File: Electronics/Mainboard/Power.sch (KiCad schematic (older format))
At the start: 7 parts

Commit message: Layout progress
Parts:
- removed TP1: TestPoint, TestPoint:TestPoint_Pad_D1.5mm, symbol Connector:TestPoint
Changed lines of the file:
@@
 	2250 4650 3100 4650
-$Comp
-L Connector:TestPoint TP1
-U 1 1 5EDB0C69
-P 2450 1150
-F 0 "TP1" H 2508 1268 50  0001 L CNN
-F 1 "TestPoint" H 2508 1177 50  0001 L CNN
-F 2 "TestPoint:TestPoint_Pad_D1.5mm" H 2650 1150 50  0001 C CNN
-F 3 "~" H 2650 1150 50  0001 C CNN
-	1    2450 1150
-	1    0    0    -1
-$EndComp
 $Comp
 L Device:CP_Small C77

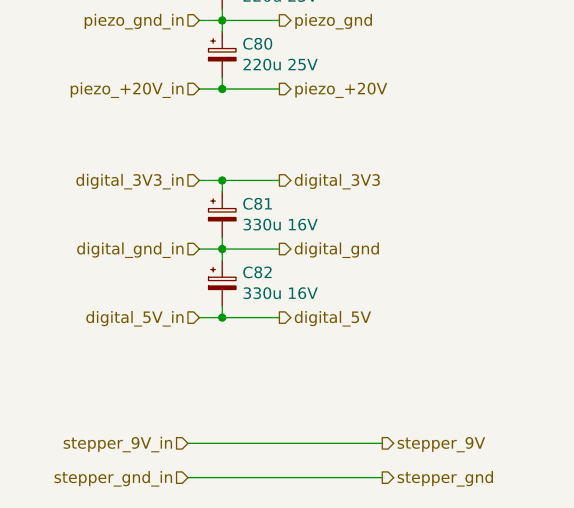
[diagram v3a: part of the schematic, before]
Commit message: Power supply routing progress
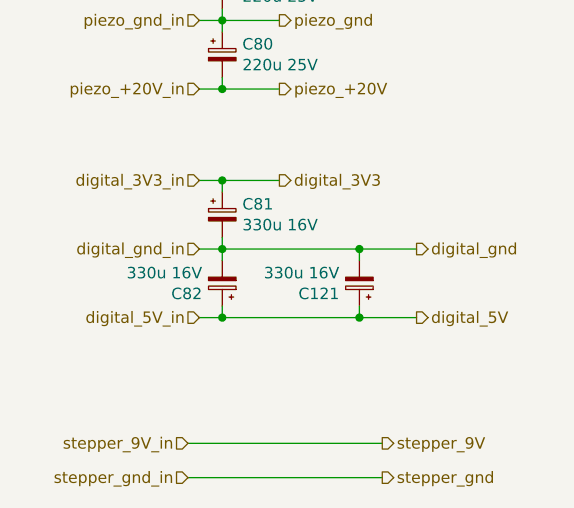
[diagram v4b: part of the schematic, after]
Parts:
- added C121: 330u 16V, Capacitor_THT:CP_Radial_D8.0mm_P3.50mm, symbol Device:CP_Small
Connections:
- net digital_5V: now also C82.1, C121.1; no longer C82.2
- net digital_gnd: now also C82.2, C121.2; no longer C82.1
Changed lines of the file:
@@
 Text HLabel 2650 3350 2    50   Output ~ 0
 digital_3V3
-Text HLabel 2650 3650 2    50   Output ~ 0
+Text HLabel 3250 3650 2    50   Output ~ 0
 digital_gnd
-Text HLabel 2650 3950 2    50   Output ~ 0
+Text HLabel 3250 3950 2    50   Output ~ 0
 digital_5V
 Text HLabel 2250 4500 0    50   Input ~ 0
@@
 	2650 3350 2400 3350
 Wire Wire Line
-	2650 3650 2400 3650
+	3250 3650 3000 3650
 Wire Wire Line
 	2300 3950 2400 3950
@@
 Connection ~ 2400 3950
 Wire Wire Line
-	2400 3950 2650 3950
+	2400 3950 3000 3950
 $Comp
 L Device:CP_Small C82
@@
 F 4 "493-1042-ND" H 2400 3800 50  0001 C CNN "Digikey"
 	1    2400 3800
-	1    0    0    -1
+	-1   0    0    1
 $EndComp
+$Comp
+L Device:CP_Small C121
+U 1 1 5EFE479A
+P 3000 3800
+F 0 "C121" H 3088 3846 50  0000 L CNN
+F 1 "330u 16V" H 3088 3755 50  0000 L CNN
+F 2 "Capacitor_THT:CP_Radial_D8.0mm_P3.50mm" H 3000 3800 50  0001 C CNN
+F 3 "~" H 3000 3800 50  0001 C CNN
+F 4 "493-1042-ND" H 3000 3800 50  0001 C CNN "Digikey"
+	1    3000 3800
+	-1   0    0    1
+$EndComp
+Wire Wire Line
+	3000 3900 3000 3950
+Connection ~ 3000 3950
+Wire Wire Line
+	3000 3950 3250 3950
+Wire Wire Line
+	3000 3700 3000 3650
+Connection ~ 3000 3650
+Wire Wire Line
+	3000 3650 2400 3650
 $EndSCHEMATC

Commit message: Layout nearly finished
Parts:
- added C122, C123, C124, C125, C126, C127, C128, C129, C130, C131, C132, C133, C134, C135, C136, C137: 1u, Capacitor_SMD:C_1210_3225Metric_Pad1.42x2.65mm_HandSolder, symbol Device:C_Small
- added TP10, TP12, TP13, TP7, TP8, TP9: TestPoint, TestPoint:TestPoint_Loop_D1.80mm_Drill1.0mm_Beaded, symbol Connector:TestPoint
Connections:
- net analog_+15V: now also C123.2, C125.2, C127.2, C129.2, C131.2, C135.2, C136.2, C137.2, TP8.1
- net analog_-15V: now also C122.1, C124.1, C126.1, C128.1, C130.1, C132.1, C133.1, C134.1, TP7.1
- net analog_gnd: now also C122.2, C123.1, C124.2, C125.1, C126.2, C127.1, C128.2, C129.1, C130.2, C131.1, C132.2, C133.2, C134.2, C135.1, C136.1, C137.1
- net digital_5V: now also TP13.1
- net piezo_+20V: now also TP10.1
- net piezo_-20V: now also TP9.1
- net stepper_9V: now also TP12.1

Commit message: Mainboard layout and schematic done
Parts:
- C122, C123, C124, C125, C126, C127, C128, C129, C130, C131, C132, C133, C134, C135, C136, C137: value 1u -> 10u; footprint Capacitor_SMD:C_1210_3225Metric_Pad1.42x2.65mm_HandSolder -> Capacitor_SMD:C_1206_3216Metric
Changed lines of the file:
@@
 P 3250 1450
 F 0 "C122" H 3342 1496 50  0000 L CNN
-F 1 "1u" H 3342 1405 50  0000 L CNN
-F 2 "Capacitor_SMD:C_1210_3225Metric_Pad1.42x2.65mm_HandSolder" H 3250 1450 50  0001 C CNN
+F 1 "10u" H 3342 1405 50  0000 L CNN
+F 2 "Capacitor_SMD:C_1206_3216Metric" H 3250 1450 50  0001 C CNN
 F 3 "~" H 3250 1450 50  0001 C CNN
 F 4 "445-13027-1-ND" H 3250 1450 50  0001 C CNN "Digikey"
+F 5 "" H 3250 1450 50  0001 C CNN "LCSC"
 	1    3250 1450
 	1    0    0    -1
@@
 P 3250 1750
 F 0 "C123" H 3342 1796 50  0000 L CNN
-F 1 "1u" H 3342 1705 50  0000 L CNN
-F 2 "Capacitor_SMD:C_1210_3225Metric_Pad1.42x2.65mm_HandSolder" H 3250 1750 50  0001 C CNN
+F 1 "10u" H 3342 1705 50  0000 L CNN
+F 2 "Capacitor_SMD:C_1206_3216Metric" H 3250 1750 50  0001 C CNN
 F 3 "~" H 3250 1750 50  0001 C CNN
 F 4 "445-13027-1-ND" H 3250 1750 50  0001 C CNN "Digikey"
+F 5 "" H 3250 1750 50  0001 C CNN "LCSC"
 	1    3250 1750
 	1    0    0    -1
@@
 P 3600 1450
 F 0 "C124" H 3692 1496 50  0000 L CNN
-F 1 "1u" H 3692 1405 50  0000 L CNN
-F 2 "Capacitor_SMD:C_1210_3225Metric_Pad1.42x2.65mm_HandSolder" H 3600 1450 50  0001 C CNN
+F 1 "10u" H 3692 1405 50  0000 L CNN
+F 2 "Capacitor_SMD:C_1206_3216Metric" H 3600 1450 50  0001 C CNN
 F 3 "~" H 3600 1450 50  0001 C CNN
 F 4 "445-13027-1-ND" H 3600 1450 50  0001 C CNN "Digikey"
+F 5 "" H 3600 1450 50  0001 C CNN "LCSC"
 	1    3600 1450
 	1    0    0    -1
@@
 P 3600 1750
 F 0 "C125" H 3692 1796 50  0000 L CNN
-F 1 "1u" H 3692 1705 50  0000 L CNN
-F 2 "Capacitor_SMD:C_1210_3225Metric_Pad1.42x2.65mm_HandSolder" H 3600 1750 50  0001 C CNN
+F 1 "10u" H 3692 1705 50  0000 L CNN
+F 2 "Capacitor_SMD:C_1206_3216Metric" H 3600 1750 50  0001 C CNN
 F 3 "~" H 3600 1750 50  0001 C CNN
 F 4 "445-13027-1-ND" H 3600 1750 50  0001 C CNN "Digikey"
+F 5 "" H 3600 1750 50  0001 C CNN "LCSC"
 	1    3600 1750
 	1    0    0    -1
@@
 P 4300 1450
 F 0 "C128" H 4392 1496 50  0000 L CNN
-F 1 "1u" H 4392 1405 50  0000 L CNN
-F 2 "Capacitor_SMD:C_1210_3225Metric_Pad1.42x2.65mm_HandSolder" H 4300 1450 50  0001 C CNN
+F 1 "10u" H 4392 1405 50  0000 L CNN
+F 2 "Capacitor_SMD:C_1206_3216Metric" H 4300 1450 50  0001 C CNN
 F 3 "~" H 4300 1450 50  0001 C CNN
 F 4 "445-13027-1-ND" H 4300 1450 50  0001 C CNN "Digikey"
+F 5 "" H 4300 1450 50  0001 C CNN "LCSC"
 	1    4300 1450
 	1    0    0    -1
@@
 P 4300 1750
 F 0 "C129" H 4392 1796 50  0000 L CNN
-F 1 "1u" H 4392 1705 50  0000 L CNN
-F 2 "Capacitor_SMD:C_1210_3225Metric_Pad1.42x2.65mm_HandSolder" H 4300 1750 50  0001 C CNN
+F 1 "10u" H 4392 1705 50  0000 L CNN
+F 2 "Capacitor_SMD:C_1206_3216Metric" H 4300 1750 50  0001 C CNN
 F 3 "~" H 4300 1750 50  0001 C CNN
 F 4 "445-13027-1-ND" H 4300 1750 50  0001 C CNN "Digikey"
+F 5 "" H 4300 1750 50  0001 C CNN "LCSC"
 	1    4300 1750
 	1    0    0    -1
@@
 P 4650 1450
 F 0 "C130" H 4742 1496 50  0000 L CNN
-F 1 "1u" H 4742 1405 50  0000 L CNN
-F 2 "Capacitor_SMD:C_1210_3225Metric_Pad1.42x2.65mm_HandSolder" H 4650 1450 50  0001 C CNN
+F 1 "10u" H 4742 1405 50  0000 L CNN
+F 2 "Capacitor_SMD:C_1206_3216Metric" H 4650 1450 50  0001 C CNN
 F 3 "~" H 4650 1450 50  0001 C CNN
 F 4 "445-13027-1-ND" H 4650 1450 50  0001 C CNN "Digikey"
+F 5 "" H 4650 1450 50  0001 C CNN "LCSC"
 	1    4650 1450
 	1    0    0    -1
@@
 P 4650 1750
 F 0 "C131" H 4742 1796 50  0000 L CNN
-F 1 "1u" H 4742 1705 50  0000 L CNN
-F 2 "Capacitor_SMD:C_1210_3225Metric_Pad1.42x2.65mm_HandSolder" H 4650 1750 50  0001 C CNN
+F 1 "10u" H 4742 1705 50  0000 L CNN
+F 2 "Capacitor_SMD:C_1206_3216Metric" H 4650 1750 50  0001 C CNN
 F 3 "~" H 4650 1750 50  0001 C CNN
 F 4 "445-13027-1-ND" H 4650 1750 50  0001 C CNN "Digikey"
+F 5 "" H 4650 1750 50  0001 C CNN "LCSC"
 	1    4650 1750
 	1    0    0    -1
@@
 P 3950 1750
 F 0 "C127" H 4042 1796 50  0000 L CNN
-F 1 "1u" H 4042 1705 50  0000 L CNN
-F 2 "Capacitor_SMD:C_1210_3225Metric_Pad1.42x2.65mm_HandSolder" H 3950 1750 50  0001 C CNN
+F 1 "10u" H 4042 1705 50  0000 L CNN
+F 2 "Capacitor_SMD:C_1206_3216Metric" H 3950 1750 50  0001 C CNN
 F 3 "~" H 3950 1750 50  0001 C CNN
 F 4 "445-13027-1-ND" H 3950 1750 50  0001 C CNN "Digikey"
+F 5 "" H 3950 1750 50  0001 C CNN "LCSC"
 	1    3950 1750
 	1    0    0    -1
@@
 P 3950 1450
 F 0 "C126" H 4042 1496 50  0000 L CNN
-F 1 "1u" H 4042 1405 50  0000 L CNN
-F 2 "Capacitor_SMD:C_1210_3225Metric_Pad1.42x2.65mm_HandSolder" H 3950 1450 50  0001 C CNN
+F 1 "10u" H 4042 1405 50  0000 L CNN
+F 2 "Capacitor_SMD:C_1206_3216Metric" H 3950 1450 50  0001 C CNN
 F 3 "~" H 3950 1450 50  0001 C CNN
 F 4 "445-13027-1-ND" H 3950 1450 50  0001 C CNN "Digikey"
+F 5 "" H 3950 1450 50  0001 C CNN "LCSC"
 	1    3950 1450
 	1    0    0    -1
@@
 P 5350 1450
 F 0 "C133" H 5442 1496 50  0000 L CNN
-F 1 "1u" H 5442 1405 50  0000 L CNN
-F 2 "Capacitor_SMD:C_1210_3225Metric_Pad1.42x2.65mm_HandSolder" H 5350 1450 50  0001 C CNN
+F 1 "10u" H 5442 1405 50  0000 L CNN
+F 2 "Capacitor_SMD:C_1206_3216Metric" H 5350 1450 50  0001 C CNN
 F 3 "~" H 5350 1450 50  0001 C CNN
 F 4 "445-13027-1-ND" H 5350 1450 50  0001 C CNN "Digikey"
+F 5 "" H 5350 1450 50  0001 C CNN "LCSC"
 	1    5350 1450
 	1    0    0    -1
@@
 P 5700 1450
 F 0 "C134" H 5792 1496 50  0000 L CNN
-F 1 "1u" H 5792 1405 50  0000 L CNN
-F 2 "Capacitor_SMD:C_1210_3225Metric_Pad1.42x2.65mm_HandSolder" H 5700 1450 50  0001 C CNN
+F 1 "10u" H 5792 1405 50  0000 L CNN
+F 2 "Capacitor_SMD:C_1206_3216Metric" H 5700 1450 50  0001 C CNN
 F 3 "~" H 5700 1450 50  0001 C CNN
 F 4 "445-13027-1-ND" H 5700 1450 50  0001 C CNN "Digikey"
+F 5 "" H 5700 1450 50  0001 C CNN "LCSC"
 	1    5700 1450
 	1    0    0    -1
@@
 P 5000 1450
 F 0 "C132" H 5092 1496 50  0000 L CNN
-F 1 "1u" H 5092 1405 50  0000 L CNN
-F 2 "Capacitor_SMD:C_1210_3225Metric_Pad1.42x2.65mm_HandSolder" H 5000 1450 50  0001 C CNN
+F 1 "10u" H 5092 1405 50  0000 L CNN
+F 2 "Capacitor_SMD:C_1206_3216Metric" H 5000 1450 50  0001 C CNN
 F 3 "~" H 5000 1450 50  0001 C CNN
 F 4 "445-13027-1-ND" H 5000 1450 50  0001 C CNN "Digikey"
+F 5 "" H 5000 1450 50  0001 C CNN "LCSC"
 	1    5000 1450
 	1    0    0    -1
@@
 P 5350 1750
 F 0 "C136" H 5442 1796 50  0000 L CNN
-F 1 "1u" H 5442 1705 50  0000 L CNN
-F 2 "Capacitor_SMD:C_1210_3225Metric_Pad1.42x2.65mm_HandSolder" H 5350 1750 50  0001 C CNN
+F 1 "10u" H 5442 1705 50  0000 L CNN
+F 2 "Capacitor_SMD:C_1206_3216Metric" H 5350 1750 50  0001 C CNN
 F 3 "~" H 5350 1750 50  0001 C CNN
 F 4 "445-13027-1-ND" H 5350 1750 50  0001 C CNN "Digikey"
+F 5 "" H 5350 1750 50  0001 C CNN "LCSC"
 	1    5350 1750
 	1    0    0    -1
@@
 P 5700 1750
 F 0 "C137" H 5792 1796 50  0000 L CNN
-F 1 "1u" H 5792 1705 50  0000 L CNN
-F 2 "Capacitor_SMD:C_1210_3225Metric_Pad1.42x2.65mm_HandSolder" H 5700 1750 50  0001 C CNN
+F 1 "10u" H 5792 1705 50  0000 L CNN
+F 2 "Capacitor_SMD:C_1206_3216Metric" H 5700 1750 50  0001 C CNN
 F 3 "~" H 5700 1750 50  0001 C CNN
 F 4 "445-13027-1-ND" H 5700 1750 50  0001 C CNN "Digikey"
+F 5 "" H 5700 1750 50  0001 C CNN "LCSC"
 	1    5700 1750
 	1    0    0    -1
@@
 P 5000 1750
 F 0 "C135" H 5092 1796 50  0000 L CNN
-F 1 "1u" H 5092 1705 50  0000 L CNN
-F 2 "Capacitor_SMD:C_1210_3225Metric_Pad1.42x2.65mm_HandSolder" H 5000 1750 50  0001 C CNN
+F 1 "10u" H 5092 1705 50  0000 L CNN
+F 2 "Capacitor_SMD:C_1206_3216Metric" H 5000 1750 50  0001 C CNN
 F 3 "~" H 5000 1750 50  0001 C CNN
 F 4 "445-13027-1-ND" H 5000 1750 50  0001 C CNN "Digikey"
+F 5 "" H 5000 1750 50  0001 C CNN "LCSC"
 	1    5000 1750
 	1    0    0    -1

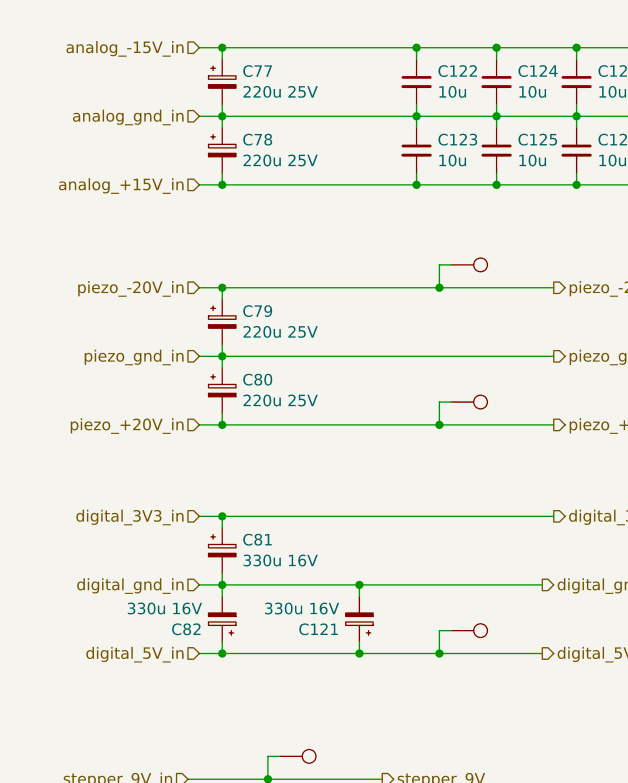
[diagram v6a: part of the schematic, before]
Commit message: Added images
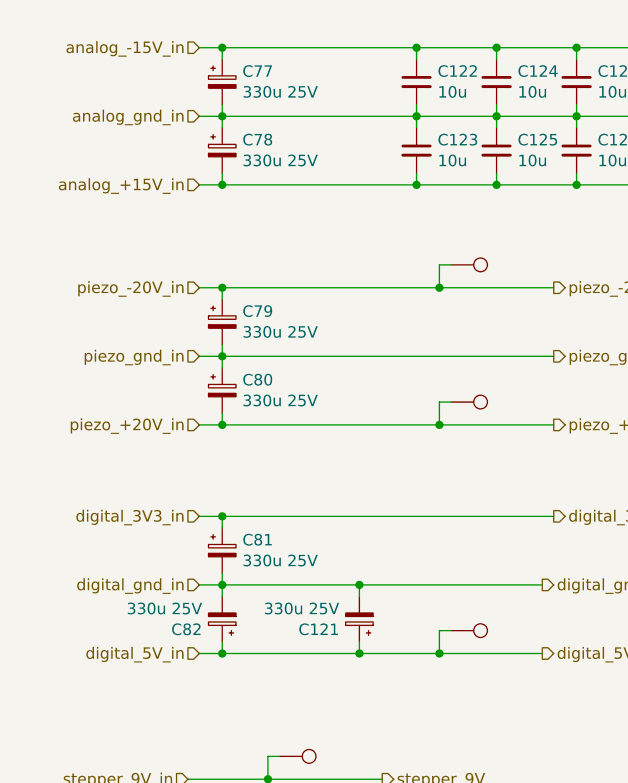
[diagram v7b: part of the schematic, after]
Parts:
- C121, C81, C82: value 330u 16V -> 330u 25V; Digikey 493-1042-ND -> (none); Reichelt (none) -> RAD FR 330/25
- C122, C123, C124, C125, C126, C127, C128, C129, C130, C131, C132, C133, C134, C135, C136, C137: Digikey 445-13027-1-ND -> (none); Reichelt (none) -> RND 1501206B475K
- C77, C78, C79, C80: value 220u 25V -> 330u 25V; Digikey 493-5914-1-ND -> (none); Reichelt (none) -> RAD FR 330/25
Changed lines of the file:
@@
 P 2400 1450
 F 0 "C77" H 2488 1496 50  0000 L CNN
-F 1 "220u 25V" H 2488 1405 50  0000 L CNN
+F 1 "330u 25V" H 2488 1405 50  0000 L CNN
 F 2 "Capacitor_THT:CP_Radial_D8.0mm_P3.50mm" H 2400 1450 50  0001 C CNN
 F 3 "~" H 2400 1450 50  0001 C CNN
-F 4 "493-5914-1-ND" H 2400 1450 50  0001 C CNN "Digikey"
+F 4 "" H 2400 1450 50  0001 C CNN "Digikey"
+F 5 "RAD FR 330/25" H 2400 1450 50  0001 C CNN "Reichelt"
 	1    2400 1450
 	1    0    0    -1
@@
 P 2400 1750
 F 0 "C78" H 2488 1796 50  0000 L CNN
-F 1 "220u 25V" H 2488 1705 50  0000 L CNN
+F 1 "330u 25V" H 2488 1705 50  0000 L CNN
 F 2 "Capacitor_THT:CP_Radial_D8.0mm_P3.50mm" H 2400 1750 50  0001 C CNN
 F 3 "~" H 2400 1750 50  0001 C CNN
-F 4 "493-5914-1-ND" H 2400 1750 50  0001 C CNN "Digikey"
+F 4 "" H 2400 1750 50  0001 C CNN "Digikey"
+F 5 "RAD FR 330/25" H 2400 1750 50  0001 C CNN "Reichelt"
 	1    2400 1750
 	1    0    0    -1
@@
 P 2400 2500
 F 0 "C79" H 2488 2546 50  0000 L CNN
-F 1 "220u 25V" H 2488 2455 50  0000 L CNN
+F 1 "330u 25V" H 2488 2455 50  0000 L CNN
 F 2 "Capacitor_THT:CP_Radial_D8.0mm_P3.50mm" H 2400 2500 50  0001 C CNN
 F 3 "~" H 2400 2500 50  0001 C CNN
-F 4 "493-5914-1-ND" H 2400 2500 50  0001 C CNN "Digikey"
+F 4 "" H 2400 2500 50  0001 C CNN "Digikey"
+F 5 "RAD FR 330/25" H 2400 2500 50  0001 C CNN "Reichelt"
 	1    2400 2500
 	1    0    0    -1
@@
 P 2400 2800
 F 0 "C80" H 2488 2846 50  0000 L CNN
-F 1 "220u 25V" H 2488 2755 50  0000 L CNN
+F 1 "330u 25V" H 2488 2755 50  0000 L CNN
 F 2 "Capacitor_THT:CP_Radial_D8.0mm_P3.50mm" H 2400 2800 50  0001 C CNN
 F 3 "~" H 2400 2800 50  0001 C CNN
-F 4 "493-5914-1-ND" H 2400 2800 50  0001 C CNN "Digikey"
+F 4 "" H 2400 2800 50  0001 C CNN "Digikey"
+F 5 "RAD FR 330/25" H 2400 2800 50  0001 C CNN "Reichelt"
 	1    2400 2800
 	1    0    0    -1
@@
 P 2400 3500
 F 0 "C81" H 2488 3546 50  0000 L CNN
-F 1 "330u 16V" H 2488 3455 50  0000 L CNN
+F 1 "330u 25V" H 2488 3455 50  0000 L CNN
 F 2 "Capacitor_THT:CP_Radial_D8.0mm_P3.50mm" H 2400 3500 50  0001 C CNN
 F 3 "~" H 2400 3500 50  0001 C CNN
-F 4 "493-1042-ND" H 2400 3500 50  0001 C CNN "Digikey"
+F 4 "" H 2400 3500 50  0001 C CNN "Digikey"
+F 5 "RAD FR 330/25" H 2400 3500 50  0001 C CNN "Reichelt"
 	1    2400 3500
 	1    0    0    -1
@@
 P 2400 3800
 F 0 "C82" H 2488 3846 50  0000 L CNN
-F 1 "330u 16V" H 2488 3755 50  0000 L CNN
+F 1 "330u 25V" H 2488 3755 50  0000 L CNN
 F 2 "Capacitor_THT:CP_Radial_D8.0mm_P3.50mm" H 2400 3800 50  0001 C CNN
 F 3 "~" H 2400 3800 50  0001 C CNN
-F 4 "493-1042-ND" H 2400 3800 50  0001 C CNN "Digikey"
+F 4 "" H 2400 3800 50  0001 C CNN "Digikey"
+F 5 "RAD FR 330/25" H 2400 3800 50  0001 C CNN "Reichelt"
 	1    2400 3800
 	-1   0    0    1
@@
 P 3000 3800
 F 0 "C121" H 3088 3846 50  0000 L CNN
-F 1 "330u 16V" H 3088 3755 50  0000 L CNN
+F 1 "330u 25V" H 3088 3755 50  0000 L CNN
 F 2 "Capacitor_THT:CP_Radial_D8.0mm_P3.50mm" H 3000 3800 50  0001 C CNN
 F 3 "~" H 3000 3800 50  0001 C CNN
-F 4 "493-1042-ND" H 3000 3800 50  0001 C CNN "Digikey"
+F 4 "" H 3000 3800 50  0001 C CNN "Digikey"
+F 5 "RAD FR 330/25" H 3000 3800 50  0001 C CNN "Reichelt"
 	1    3000 3800
 	-1   0    0    1
@@
 F 2 "Capacitor_SMD:C_1206_3216Metric" H 3250 1450 50  0001 C CNN
 F 3 "~" H 3250 1450 50  0001 C CNN
-F 4 "445-13027-1-ND" H 3250 1450 50  0001 C CNN "Digikey"
+F 4 "" H 3250 1450 50  0001 C CNN "Digikey"
 F 5 "" H 3250 1450 50  0001 C CNN "LCSC"
+F 6 "RND 1501206B475K" H 3250 1450 50  0001 C CNN "Reichelt"
 	1    3250 1450
 	1    0    0    -1
@@
 F 2 "Capacitor_SMD:C_1206_3216Metric" H 3250 1750 50  0001 C CNN
 F 3 "~" H 3250 1750 50  0001 C CNN
-F 4 "445-13027-1-ND" H 3250 1750 50  0001 C CNN "Digikey"
+F 4 "" H 3250 1750 50  0001 C CNN "Digikey"
 F 5 "" H 3250 1750 50  0001 C CNN "LCSC"
+F 6 "RND 1501206B475K" H 3250 1750 50  0001 C CNN "Reichelt"
 	1    3250 1750
 	1    0    0    -1
@@
 F 2 "Capacitor_SMD:C_1206_3216Metric" H 3600 1450 50  0001 C CNN
 F 3 "~" H 3600 1450 50  0001 C CNN
-F 4 "445-13027-1-ND" H 3600 1450 50  0001 C CNN "Digikey"
+F 4 "" H 3600 1450 50  0001 C CNN "Digikey"
 F 5 "" H 3600 1450 50  0001 C CNN "LCSC"
+F 6 "RND 1501206B475K" H 3600 1450 50  0001 C CNN "Reichelt"
 	1    3600 1450
 	1    0    0    -1
@@
 F 2 "Capacitor_SMD:C_1206_3216Metric" H 3600 1750 50  0001 C CNN
 F 3 "~" H 3600 1750 50  0001 C CNN
-F 4 "445-13027-1-ND" H 3600 1750 50  0001 C CNN "Digikey"
+F 4 "" H 3600 1750 50  0001 C CNN "Digikey"
 F 5 "" H 3600 1750 50  0001 C CNN "LCSC"
+F 6 "RND 1501206B475K" H 3600 1750 50  0001 C CNN "Reichelt"
 	1    3600 1750
 	1    0    0    -1
@@
 F 2 "Capacitor_SMD:C_1206_3216Metric" H 4300 1450 50  0001 C CNN
 F 3 "~" H 4300 1450 50  0001 C CNN
-F 4 "445-13027-1-ND" H 4300 1450 50  0001 C CNN "Digikey"
+F 4 "" H 4300 1450 50  0001 C CNN "Digikey"
 F 5 "" H 4300 1450 50  0001 C CNN "LCSC"
+F 6 "RND 1501206B475K" H 4300 1450 50  0001 C CNN "Reichelt"
 	1    4300 1450
 	1    0    0    -1
@@
 F 2 "Capacitor_SMD:C_1206_3216Metric" H 4300 1750 50  0001 C CNN
 F 3 "~" H 4300 1750 50  0001 C CNN
-F 4 "445-13027-1-ND" H 4300 1750 50  0001 C CNN "Digikey"
+F 4 "" H 4300 1750 50  0001 C CNN "Digikey"
 F 5 "" H 4300 1750 50  0001 C CNN "LCSC"
+F 6 "RND 1501206B475K" H 4300 1750 50  0001 C CNN "Reichelt"
 	1    4300 1750
 	1    0    0    -1
@@
 F 2 "Capacitor_SMD:C_1206_3216Metric" H 4650 1450 50  0001 C CNN
 F 3 "~" H 4650 1450 50  0001 C CNN
-F 4 "445-13027-1-ND" H 4650 1450 50  0001 C CNN "Digikey"
+F 4 "" H 4650 1450 50  0001 C CNN "Digikey"
 F 5 "" H 4650 1450 50  0001 C CNN "LCSC"
+F 6 "RND 1501206B475K" H 4650 1450 50  0001 C CNN "Reichelt"
 	1    4650 1450
 	1    0    0    -1
@@
 F 2 "Capacitor_SMD:C_1206_3216Metric" H 4650 1750 50  0001 C CNN
 F 3 "~" H 4650 1750 50  0001 C CNN
-F 4 "445-13027-1-ND" H 4650 1750 50  0001 C CNN "Digikey"
+F 4 "" H 4650 1750 50  0001 C CNN "Digikey"
 F 5 "" H 4650 1750 50  0001 C CNN "LCSC"
+F 6 "RND 1501206B475K" H 4650 1750 50  0001 C CNN "Reichelt"
 	1    4650 1750
 	1    0    0    -1
@@
 F 2 "Capacitor_SMD:C_1206_3216Metric" H 3950 1750 50  0001 C CNN
 F 3 "~" H 3950 1750 50  0001 C CNN
-F 4 "445-13027-1-ND" H 3950 1750 50  0001 C CNN "Digikey"
+F 4 "" H 3950 1750 50  0001 C CNN "Digikey"
 F 5 "" H 3950 1750 50  0001 C CNN "LCSC"
+F 6 "RND 1501206B475K" H 3950 1750 50  0001 C CNN "Reichelt"
 	1    3950 1750
 	1    0    0    -1
@@
 F 2 "Capacitor_SMD:C_1206_3216Metric" H 3950 1450 50  0001 C CNN
 F 3 "~" H 3950 1450 50  0001 C CNN
-F 4 "445-13027-1-ND" H 3950 1450 50  0001 C CNN "Digikey"
+F 4 "" H 3950 1450 50  0001 C CNN "Digikey"
 F 5 "" H 3950 1450 50  0001 C CNN "LCSC"
+F 6 "RND 1501206B475K" H 3950 1450 50  0001 C CNN "Reichelt"
 	1    3950 1450
 	1    0    0    -1
@@
 F 2 "Capacitor_SMD:C_1206_3216Metric" H 5350 1450 50  0001 C CNN
 F 3 "~" H 5350 1450 50  0001 C CNN
-F 4 "445-13027-1-ND" H 5350 1450 50  0001 C CNN "Digikey"
+F 4 "" H 5350 1450 50  0001 C CNN "Digikey"
 F 5 "" H 5350 1450 50  0001 C CNN "LCSC"
+F 6 "RND 1501206B475K" H 5350 1450 50  0001 C CNN "Reichelt"
 	1    5350 1450
 	1    0    0    -1
@@
 F 2 "Capacitor_SMD:C_1206_3216Metric" H 5700 1450 50  0001 C CNN
 F 3 "~" H 5700 1450 50  0001 C CNN
-F 4 "445-13027-1-ND" H 5700 1450 50  0001 C CNN "Digikey"
+F 4 "" H 5700 1450 50  0001 C CNN "Digikey"
 F 5 "" H 5700 1450 50  0001 C CNN "LCSC"
+F 6 "RND 1501206B475K" H 5700 1450 50  0001 C CNN "Reichelt"
 	1    5700 1450
 	1    0    0    -1
@@
 F 2 "Capacitor_SMD:C_1206_3216Metric" H 5000 1450 50  0001 C CNN
 F 3 "~" H 5000 1450 50  0001 C CNN
-F 4 "445-13027-1-ND" H 5000 1450 50  0001 C CNN "Digikey"
+F 4 "" H 5000 1450 50  0001 C CNN "Digikey"
 F 5 "" H 5000 1450 50  0001 C CNN "LCSC"
+F 6 "RND 1501206B475K" H 5000 1450 50  0001 C CNN "Reichelt"
 	1    5000 1450
 	1    0    0    -1
@@
 F 2 "Capacitor_SMD:C_1206_3216Metric" H 5350 1750 50  0001 C CNN
 F 3 "~" H 5350 1750 50  0001 C CNN
-F 4 "445-13027-1-ND" H 5350 1750 50  0001 C CNN "Digikey"
+F 4 "" H 5350 1750 50  0001 C CNN "Digikey"
 F 5 "" H 5350 1750 50  0001 C CNN "LCSC"
+F 6 "RND 1501206B475K" H 5350 1750 50  0001 C CNN "Reichelt"
 	1    5350 1750
 	1    0    0    -1
@@
 F 2 "Capacitor_SMD:C_1206_3216Metric" H 5700 1750 50  0001 C CNN
 F 3 "~" H 5700 1750 50  0001 C CNN
-F 4 "445-13027-1-ND" H 5700 1750 50  0001 C CNN "Digikey"
+F 4 "" H 5700 1750 50  0001 C CNN "Digikey"
 F 5 "" H 5700 1750 50  0001 C CNN "LCSC"
+F 6 "RND 1501206B475K" H 5700 1750 50  0001 C CNN "Reichelt"
 	1    5700 1750
 	1    0    0    -1
@@
 F 2 "Capacitor_SMD:C_1206_3216Metric" H 5000 1750 50  0001 C CNN
 F 3 "~" H 5000 1750 50  0001 C CNN
-F 4 "445-13027-1-ND" H 5000 1750 50  0001 C CNN "Digikey"
+F 4 "" H 5000 1750 50  0001 C CNN "Digikey"
 F 5 "" H 5000 1750 50  0001 C CNN "LCSC"
+F 6 "RND 1501206B475K" H 5000 1750 50  0001 C CNN "Reichelt"
 	1    5000 1750
 	1    0    0    -1
